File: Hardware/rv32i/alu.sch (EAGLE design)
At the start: 142 parts, among them IC1 SN74HCS86DR, IC10 SN74HCS86DR, IC11 SN74HCS86DR, IC12 SN74HCS86DR, IC13 SN74HCS86DR, IC14 SN74HCS86DR, IC15 SN74HCS86DR, IC16 SN74HCS86DR, IC17 SN74HCS86DR, IC18 SN74HCS86DR, IC19 SN74HCS86DR, IC2 SN74HCS86DR, IC20 SN74HCS86DR, IC21 SN74HCS86DR, IC22 SN74HCS86DR, IC23 SN74HCS86DR, IC24 SN74HCS86DR, IC25 SN74ACT08D, IC26 SN74ACT08D, IC27 SN74ACT08D, IC28 SN74ACT08D, IC29 SN74ACT08D, IC3 SN74HCS86DR, IC30 SN74ACT08D, IC31 SN74ACT08D, IC32 SN74ACT08D, IC33 SN74ACT08D, IC34 SN74ACT08D, IC35 SN74ACT08D, IC36 SN74ACT08D, IC37 SN74ACT08D, IC38 SN74ACT08D, IC39 SN74ACT08D, IC4 SN74HCS86DR, IC40 SN74ACT08D, IC41 SN74HCS32DR, IC42 SN74HCS32DR, IC43 SN74HCS32DR, IC44 SN74HCS32DR, IC45 SN74HCS32DR, IC46 SN74HCS32DR, IC47 SN74HCS32DR, IC48 SN74HCS32DR, IC5 SN74HCS86DR, IC6 SN74HCS86DR, IC7 SN74HCS86DR, IC8 SN74HCS86DR, IC9 SN74HCS86DR

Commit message: Resistors
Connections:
- removed net N$1: IC1.GND
- removed net N$106: IC8.VCC
- removed net N$113: IC9.GND
- removed net N$120: IC9.VCC
- removed net N$127: IC10.GND
- removed net N$134: IC10.VCC
- removed net N$141: IC11.GND
- removed net N$148: IC11.VCC
- removed net N$15: IC2.GND
- removed net N$155: IC12.GND
- removed net N$162: IC12.VCC
- removed net N$169: IC13.GND
- removed net N$176: IC13.VCC
- removed net N$183: IC14.GND
- removed net N$190: IC14.VCC
- removed net N$197: IC15.GND
- removed net N$204: IC15.VCC
- removed net N$211: IC16.GND
- removed net N$218: IC16.VCC
- removed net N$22: IC2.VCC
- removed net N$231: IC33.GND
- removed net N$238: IC33.VCC
- removed net N$245: IC34.GND
- removed net N$252: IC34.VCC
- removed net N$259: IC35.GND
- removed net N$266: IC35.VCC
- removed net N$273: IC36.GND
- removed net N$280: IC36.VCC
- removed net N$287: IC37.GND
- removed net N$294: IC37.VCC
- removed net N$3: IC3.VCC
- removed net N$301: IC38.GND
- removed net N$308: IC38.VCC
- removed net N$315: IC39.GND
- removed net N$329: IC40.GND
- removed net N$336: IC40.VCC
- removed net N$343: IC41.GND
- removed net N$344: IC41.VCC
- removed net N$345: IC17.GND
- removed net N$352: IC17.VCC
- removed net N$359: IC18.GND
- removed net N$366: IC18.VCC
- removed net N$373: IC19.GND
- removed net N$380: IC19.VCC
- removed net N$387: IC20.GND
- removed net N$394: IC20.VCC
- removed net N$401: IC21.GND
- removed net N$408: IC21.VCC
- removed net N$415: IC22.GND
- removed net N$422: IC22.VCC
- removed net N$429: IC23.GND
- removed net N$43: IC4.GND
- removed net N$436: IC23.VCC
- removed net N$443: IC24.GND
- removed net N$450: IC24.VCC
- removed net N$463: IC25.GND
- removed net N$470: IC25.VCC
- removed net N$477: IC26.GND
- removed net N$484: IC26.VCC
- removed net N$491: IC27.GND
- removed net N$498: IC27.VCC
- removed net N$50: IC4.VCC
- removed net N$505: IC28.GND
- removed net N$512: IC28.VCC
- removed net N$519: IC29.GND
- removed net N$526: IC29.VCC
- removed net N$533: IC30.GND
- removed net N$540: IC30.VCC
- removed net N$547: IC31.GND
- removed net N$554: IC31.VCC
- removed net N$561: IC32.GND
- removed net N$568: IC32.VCC
- removed net N$57: IC5.GND
- removed net N$64: IC5.VCC
- removed net N$701: IC42.GND
- removed net N$702: IC42.VCC
- removed net N$71: IC6.GND
- removed net N$715: IC43.GND
- removed net N$716: IC43.VCC
- removed net N$729: IC44.GND
- removed net N$730: IC44.VCC
- removed net N$743: IC45.GND
- removed net N$744: IC45.VCC
- removed net N$757: IC46.GND
- removed net N$758: IC46.VCC
- removed net N$771: IC47.GND
- removed net N$772: IC47.VCC
- removed net N$78: IC6.VCC
- removed net N$785: IC48.GND
- removed net N$786: IC48.VCC
- removed net N$8: IC1.VCC
- removed net N$85: IC7.GND
- removed net N$92: IC7.VCC
- removed net N$99: IC8.GND
- net D1_B11: no longer R12.1
- net D1_B12: now also R12.1
- net D1_B15: no longer IC39.VCC
- net D2_B24: no longer R58.1
- net D2_B25: now also R58.1
- net D2_B30: no longer JP1.34, JP4.34
- net D2_B31: now also JP1.34, JP4.34
- net GND: now also IC1.GND, IC10.GND, IC11.GND, IC12.GND, IC13.GND, IC14.GND, IC15.GND, IC16.GND, IC17.GND, IC18.GND, IC19.GND, IC2.GND, IC20.GND, IC21.GND, IC22.GND, IC23.GND, IC24.GND, IC25.GND, IC26.GND, IC27.GND, IC28.GND, IC29.GND, IC3.GND, IC30.GND, IC31.GND, IC32.GND, IC33.GND, IC34.GND, IC35.GND, IC36.GND, IC37.GND, IC38.GND, IC39.GND, IC4.GND, IC40.GND, IC41.GND, IC42.GND, IC43.GND, IC44.GND, IC45.GND, IC46.GND, IC47.GND, IC48.GND, IC5.GND, IC6.GND, IC7.GND, IC8.GND, IC9.GND
- net SUM_B5: no longer JP5.15, JP6.15
- net SUM_B6: now also JP5.15, JP6.15
- net VCC: now also IC1.VCC, IC10.VCC, IC11.VCC, IC12.VCC, IC13.VCC, IC14.VCC, IC15.VCC, IC16.VCC, IC17.VCC, IC18.VCC, IC19.VCC, IC2.VCC, IC20.VCC, IC21.VCC, IC22.VCC, IC23.VCC, IC24.VCC, IC25.VCC, IC26.VCC, IC27.VCC, IC28.VCC, IC29.VCC, IC3.VCC, IC30.VCC, IC31.VCC, IC32.VCC, IC33.VCC, IC34.VCC, IC35.VCC, IC36.VCC, IC37.VCC, IC38.VCC, IC39.VCC, IC4.VCC, IC40.VCC, IC41.VCC, IC42.VCC, IC43.VCC, IC44.VCC, IC45.VCC, IC46.VCC, IC47.VCC, IC48.VCC, IC5.VCC, IC6.VCC, IC7.VCC, IC8.VCC, IC9.VCC
- net XOR_B6: no longer IC3.GND

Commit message: Alu design
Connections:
- removed net N$2: C1.2, C10.2, C11.2, C12.2, C13.2, C14.2, C15.2, C16.2, C17.2, C18.2, C19.2, C2.2, C20.2, C21.2, C22.2, C23.2, C24.2, C3.2, C4.2, C5.2, C6.2, C7.2, C8.2, C9.2
- removed net N$30: IC3.2Y
- net VCC: now also C1.2, C10.2, C11.2, C12.2, C13.2, C14.2, C15.2, C16.2, C17.2, C18.2, C19.2, C2.2, C20.2, C21.2, C22.2, C23.2, C24.2, C3.2, C4.2, C5.2, C6.2, C7.2, C8.2, C9.2
- net XOR_B6: now also IC3.2Y

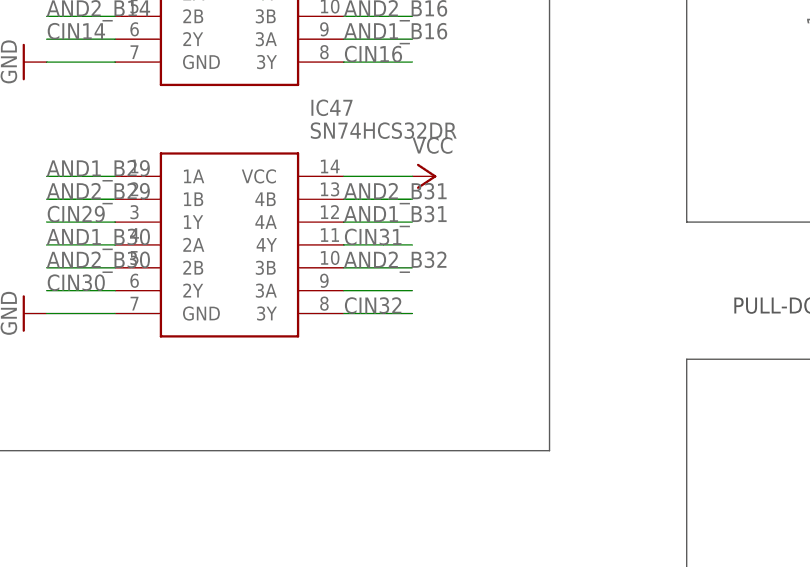
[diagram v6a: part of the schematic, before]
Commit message: Modify ALU & Libraries
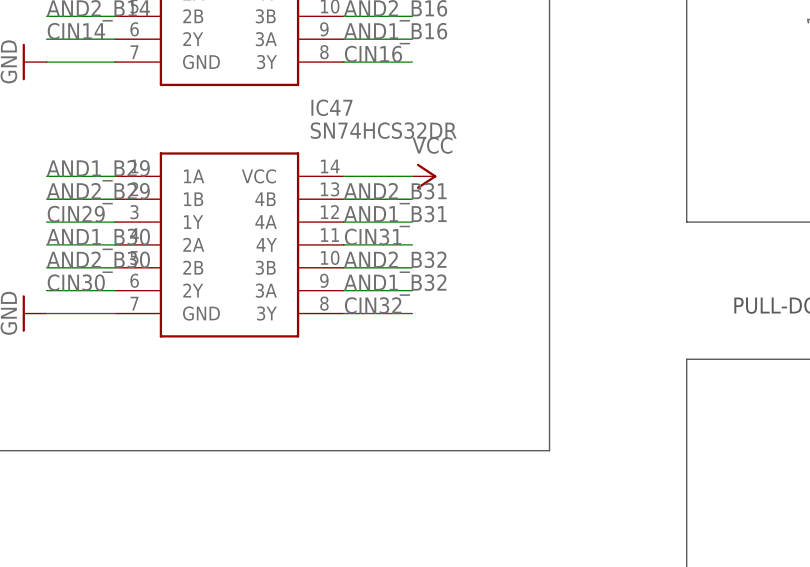
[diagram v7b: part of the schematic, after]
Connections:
- removed net AND1_B33: IC47.3A
- net AND1_B32: now also IC47.3A
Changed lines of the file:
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@@
 <label x="459.74" y="109.22" size="1.778" layer="95"/>
+</segment>
+<segment>
+<pinref part="IC47" gate="G$1" pin="3A"/>
+<wire x1="457.2" y1="205.74" x2="464.82" y2="205.74" width="0.1524" layer="91"/>
+<label x="457.2" y="205.74" size="1.778" layer="95"/>
 </segment>
 </net>
@@
 </segment>
 </net>
-<net name="AND1_B33" class="0">
-<segment>
-<pinref part="IC47" gate="G$1" pin="3A"/>
-<wire x1="457.2" y1="205.74" x2="464.82" y2="205.74" width="0.1524" layer="91"/>
-</segment>
-</net>
 <net name="CIN32" class="0">
 <segment>
@@
 </sheet>
 </sheets>
+<errors>
+</errors>
 </schematic>
 </drawing>
